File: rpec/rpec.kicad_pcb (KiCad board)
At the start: 2 copper layers, 65 x 56 mm, 35 parts, among them J1 GPIO, J10 Conn_02x04_Odd_Even, J11 Conn_02x04_Odd_Even, J12 Conn_02x03_Odd_Even, J2 Conn_01x02_Pin, J3 Conn_01x03_Pin, J4 Conn_02x03_Odd_Even, J5 Conn_01x04_Male, J6 Conn_01x04_Male, J7 Conn_01x03_Pin, J8 Conn_01x03_Pin, J9 Conn_01x04_Pin, M1 Fan, U1 CAT24C256, U2 PCF8563T, U3 MCP3428x-xSL, Y1 Crystal_GND3

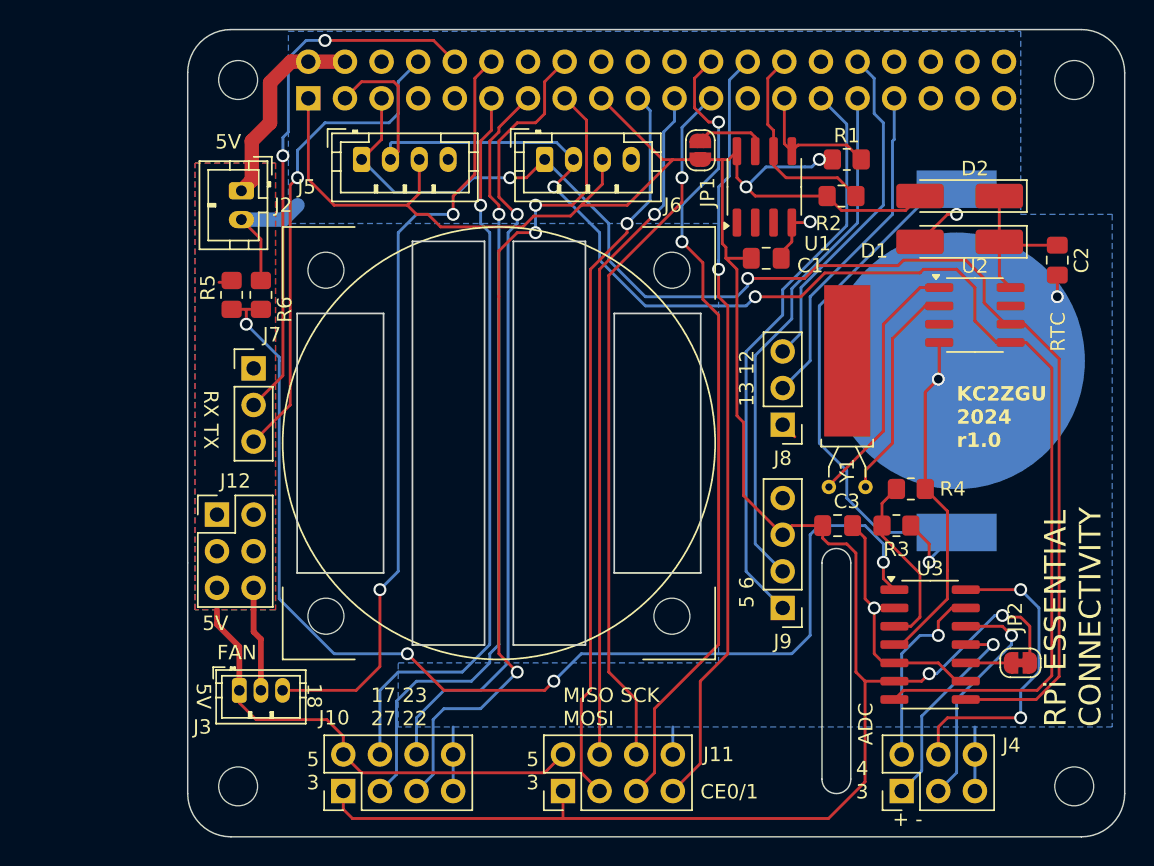
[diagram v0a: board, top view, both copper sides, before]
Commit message: rpec: r1.1 (WIP)
 - Add Pi 5-compatible fan header
 - Move RTC components and use SMD crystal
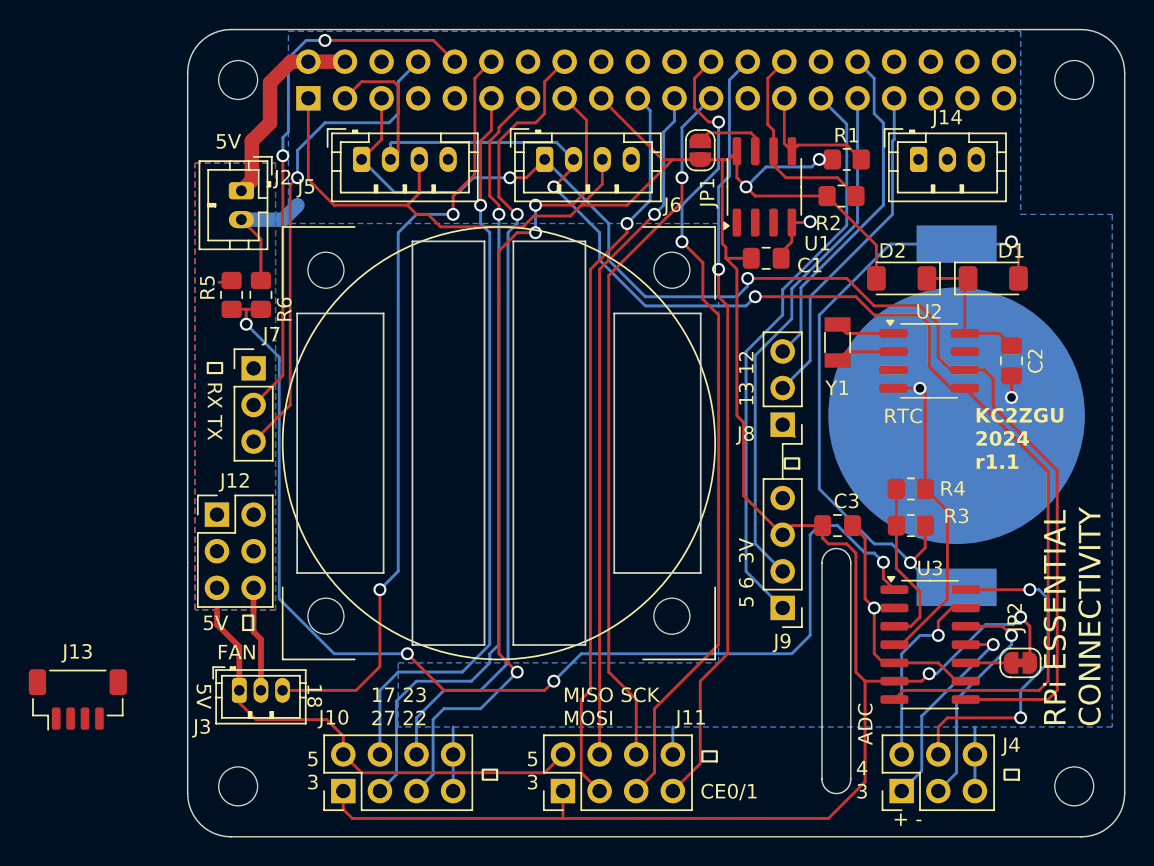
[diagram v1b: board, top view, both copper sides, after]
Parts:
- added J13: Conn_01x04_Pin, Connector_JST:JST_SH_BM04B-SRSS-TB_1x04-1MP_P1.00mm_Vertical, F.Cu at (92.4, 90.5)
- added J14: Conn_01x03_Pin, Connector_JST:JST_PH_B3B-PH-K_1x03_P2.00mm_Vertical, F.Cu at (150.7, 53.0)
- D1, D2: footprint Diode_SMD:D_MiniMELF_Handsoldering -> Diode_SMD:D_MiniMELF
- R3, R4: value R_US -> 100K 1%
- R5: value R_US -> 30K 1%
- R6: value R_US -> 10K 1%
- Y1: value Crystal_GND3 -> Crystal; footprint Crystal:Crystal_AT310_D3.0mm_L10.0mm_Horizontal_1EP_style1 -> Crystal:Crystal_SMD_3215-2Pin_3.2x1.5mm
- moved Y1 10.2 mm to (145.1, 65.7), turned to -90 degrees
- moved C2 7.67 mm to (157.2, 67.0)
- moved D2 6.99 mm to (149.5, 61.3)
- moved U2 4.49 mm to (151.4, 67.0)
- moved BT1 3.81 mm to (153.3, 70.8)
- moved D1 3.45 mm to (155.9, 61.3), turned to 0 degrees
- moved R3 1.00 mm to (150.2, 78.4)
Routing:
- net Net-(U2-OSCI): track 17.7 -> 4.13 mm
- net Net-(U2-OSCO): track 15.2 -> 4.13 mm
- net /GPIO2/SDA1: track 103.6 -> 97.9 mm
- net /GPIO3/SCL1: track 94.9 -> 91.1 mm
- net GND: track 76.3 -> 74.7 mm
- net /AD4n: track 21.6 -> 22.9 mm
- net Net-(BT1-+): track 46.6 -> 45.6 mm
- net /AD2p: track 12.4 -> 11.6 mm
- net /AD1p: track 80.4 -> 79.7 mm
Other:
- board text added: "5 6 3V"
- board text added: "5V ⏚"
- board text added: "KC2ZGU 2024 r1.1"
- board text added: "⏚"
- board text added: "⏚ RX TX"
- board text removed: "5 6"
- board text removed: "KC2ZGU 2024 r1.0"
- board text removed: "RX TX"

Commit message: rpec: r1.1
 - Connect Pi 5 fan header
 - RTC voltage header
 - Header for Alternate ADC 1/2 inputs
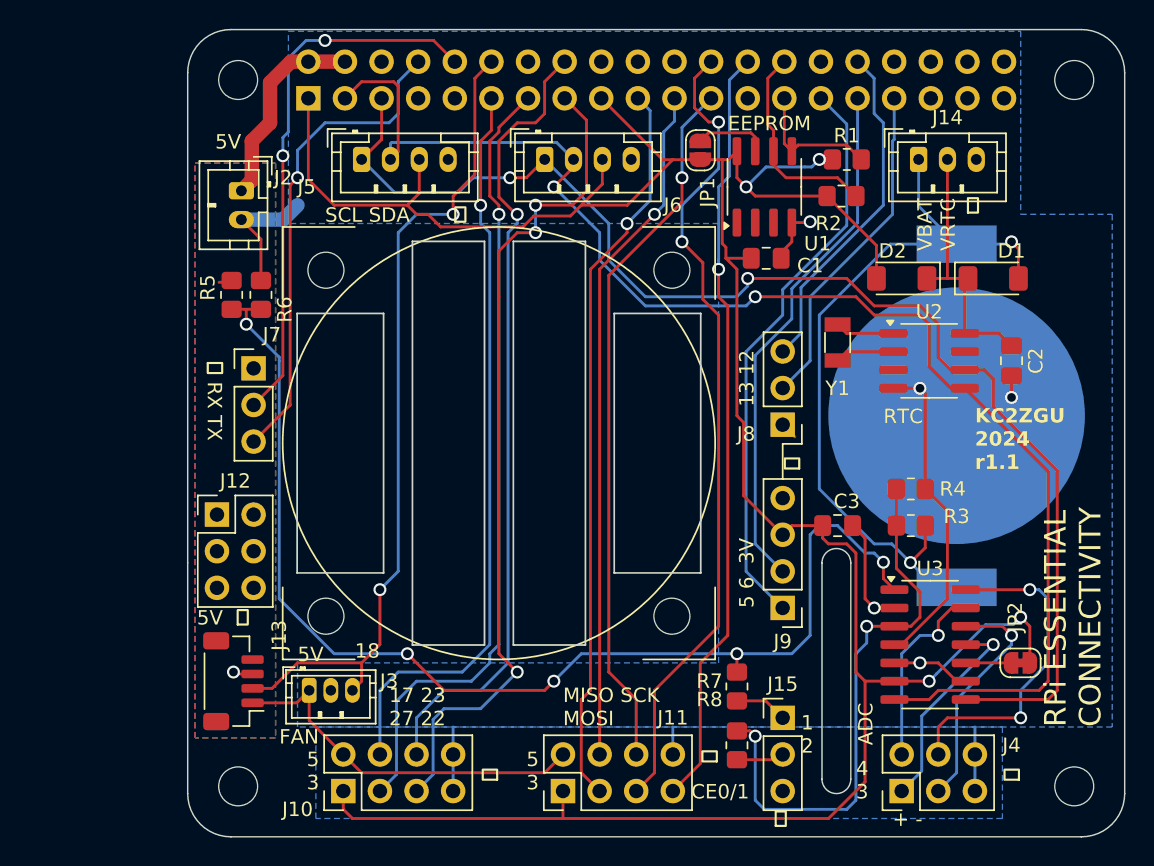
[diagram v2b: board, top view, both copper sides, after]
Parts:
- added J15: Conn_01x03_Pin, Connector_PinHeader_2.54mm:PinHeader_1x03_P2.54mm_Vertical, F.Cu at (141.3, 91.7)
- added R7: 30K 1%, Resistor_SMD:R_0805_2012Metric_Pad1.20x1.40mm_HandSolder, F.Cu at (138.1, 89.6)
- added R8: 100K 1%, Resistor_SMD:R_0805_2012Metric_Pad1.20x1.40mm_HandSolder, F.Cu at (138.1, 93.7)
- moved J13 10.9 mm to (103.2, 89.2), turned to 90 degrees
- moved J3 4.85 mm to (108.4, 89.8)
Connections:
- BT1 pad 1: Net-(BT1-+) -> /VBAT
- C2 pad 1: Net-(D1-K) -> /VRTC
- D1 pad 1: Net-(D1-K) -> /VRTC
- D1 pad 2: Net-(BT1-+) -> /VBAT
- D2 pad 1: Net-(D1-K) -> /VRTC
- J14 pad 1: unconnected-(J14-Pin_1-Pad1) -> /VBAT
- J14 pad 2: unconnected-(J14-Pin_2-Pad2) -> /VRTC
- J14 pad 3: unconnected-(J14-Pin_3-Pad3) -> GND
- R3 pad 1: Net-(BT1-+) -> /VBAT
- U2 pad 8: Net-(D1-K) -> /VRTC
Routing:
- net /VBAT: track 0.00 -> 52.6 mm, vias 0 -> 2
- net Net-(BT1-+): track 45.6 -> 0.00 mm, vias 2 -> 0
- net /AD2p: track 11.6 -> 39.3 mm, vias 0 -> 2
- net /VRTC: track 0.00 -> 18.6 mm
- net Net-(D1-K): track 10.4 -> 0.00 mm
- net GND: track 74.7 -> 64.7 mm, vias 4 -> 6
- net +5V: track 48.0 -> 41.1 mm
- net Net-(J15-Pin_1): track 0.00 -> 3.66 mm
- net Net-(J15-Pin_2): track 0.00 -> 3.33 mm
- net /GPIO18/PCM.CLK: track 54.1 -> 57.4 mm
- net /AD1p: track 79.7 -> 81.0 mm, vias 4 -> 5
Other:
- board text added: "1 2"
- board text added: "EEPROM"
- board text added: "SCL SDA"
- board text added: "VBAT VRTC"
